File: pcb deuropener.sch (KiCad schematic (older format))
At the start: 30 parts, among them J1 Conn_01x02, J10 Conn_01x03, J11 Barrel_Jack_Switch, J12 Conn_01x08, J13 Conn_01x02, J14 Conn_01x02, J2 Conn_01x02, J3 Conn_01x02, J4 Conn_01x02, J8 Conn_01x02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

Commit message: A lot of changes to rev 0.02
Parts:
- removed J8: Conn_01x02, Connector_PinHeader_2.54mm:PinHeader_1x02_P2.54mm_Vertical, symbol Connector_Generic:Conn_01x02
- removed R11: R, Resistor_THT:R_Axial_DIN0207_L6.3mm_D2.5mm_P10.16mm_Horizontal, symbol Device:R
- added D3: LED, LED_THT:LED_D5.0mm, symbol Device:LED
- added D4: 1N4007, Diode_THT:D_DO-41_SOD81_P10.16mm_Horizontal, symbol Diode:1N4007
- added J5: Conn_01x02, Connector_PinHeader_2.54mm:PinHeader_1x02_P2.54mm_Vertical, symbol Connector_Generic:Conn_01x02
- added Q2: STU60N3LH5, Package_TO_SOT_THT:SIPAK_Vertical, symbol Device:Q_NMOS_GDS
- added R7, R8: R, Resistor_THT:R_Axial_DIN0207_L6.3mm_D2.5mm_P10.16mm_Horizontal, symbol Device:R
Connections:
- net +12V: now also D4.1 (K), J5.1 (Pin_1)
- net Earth: now also D3.1 (K), Q2.3 (S)
- net IO-P9_12-Solenoid: now reaches P9.12 (Pin_12)
- net IO-P9_12-Solenoid: now also R16.1, R17.1
- net IO-P9_16-UILED2: now reaches P9.16 (Pin_16)
- net IO-P9_16-UILED2: now also R4.1
- net IO-P8_13-UI_TriLED1r: now reaches P8.13 (Pin_13)
- net IO-P8_13-UI_TriLED1r: now also R14.2
- net IO-P8_17-Button1: now reaches P8.17 (Pin_17)
- net IO-P8_17-Button1: now also C2.2, R5.2, R6.1
- net IO-P8_18-Button2: now reaches P8.18 (Pin_18)
- net IO-P8_18-Button2: now also C1.2, R2.2, R3.1
- net IO-P8_19-UI_TriLED1g: now reaches P8.19 (Pin_19)
- net IO-P8_19-UI_TriLED1g: now also R15.2
- net IO-P8_09-Buzzer: now reaches P8.9 (Pin_9)
- net IO-P8_09-Buzzer: now also R7.1, R8.1
- removed net IO-P8_21-Button2: C1.2, P8.21 (Pin_21), R2.2, R3.1
- removed net IO-P8_23-Button1: C2.2, P8.23 (Pin_23), R5.2, R6.1
- net IO-P8_34-UILED1: no longer names the net of P8.34 (Pin_34)
- net IO-P8_34-UILED1: no longer R1.1
- net IO-P8_36-UILED2: no longer names the net of P8.36 (Pin_36)
- net IO-P8_36-UILED2: no longer R4.1
- net IO-P8_45-UI_BiLED1g: no longer names the net of P8.45 (Pin_45)
- net IO-P8_46-UI_BiLED1r: no longer names the net of P8.46 (Pin_46)
- removed net IO-P9_14-Solenoid: P9.14 (Pin_14), R16.1, R17.1
- net IO-P9_28-UI_TriLED1r: no longer names the net of P9.28 (Pin_28)
- net IO-P9_28-UI_TriLED1r: no longer R14.2
- net IO-P9_42-UI_TriLED1g: no longer names the net of P9.42 (Pin_42)
- net IO-P9_42-UI_TriLED1g: no longer R15.2
- new net: D3.2 (A), R7.2
- new net: Q2.1 (G), R8.2
- new net: D4.2 (A), J5.2 (Pin_2), Q2.2 (D)
- new net IO-P9_14-UILED1: P9.14 (Pin_14), R1.1
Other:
- note added: "Buzzer 12V"
- note added: "Doorbell (button2)"
- note added: "intercom door open switch \n(Button1)"
- note removed: "Button 1"
- note removed: "Button 2"
- note removed: "UI bicolor LED"
- moved on the sheet: C3, D1, D2, J10, J13, Q1, R14, R15, R16, R17

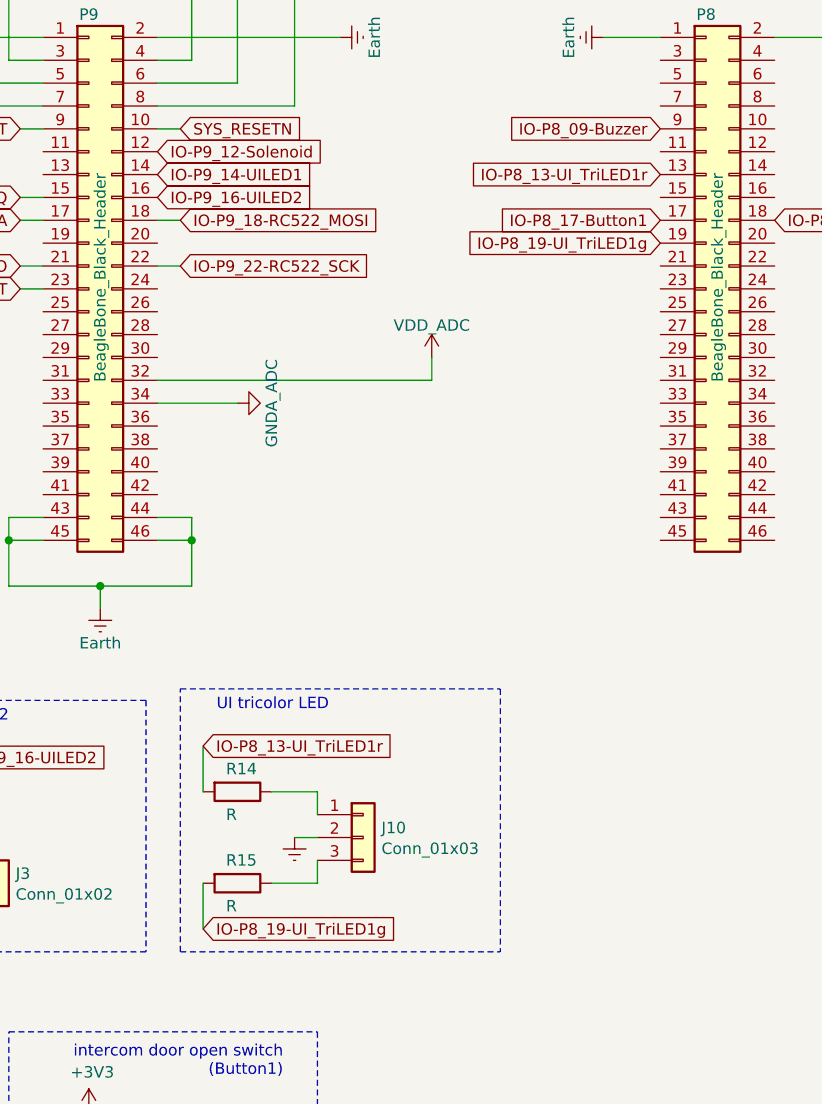
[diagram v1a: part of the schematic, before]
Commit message: A lot of changes for rev0.02 and fix for issue #2
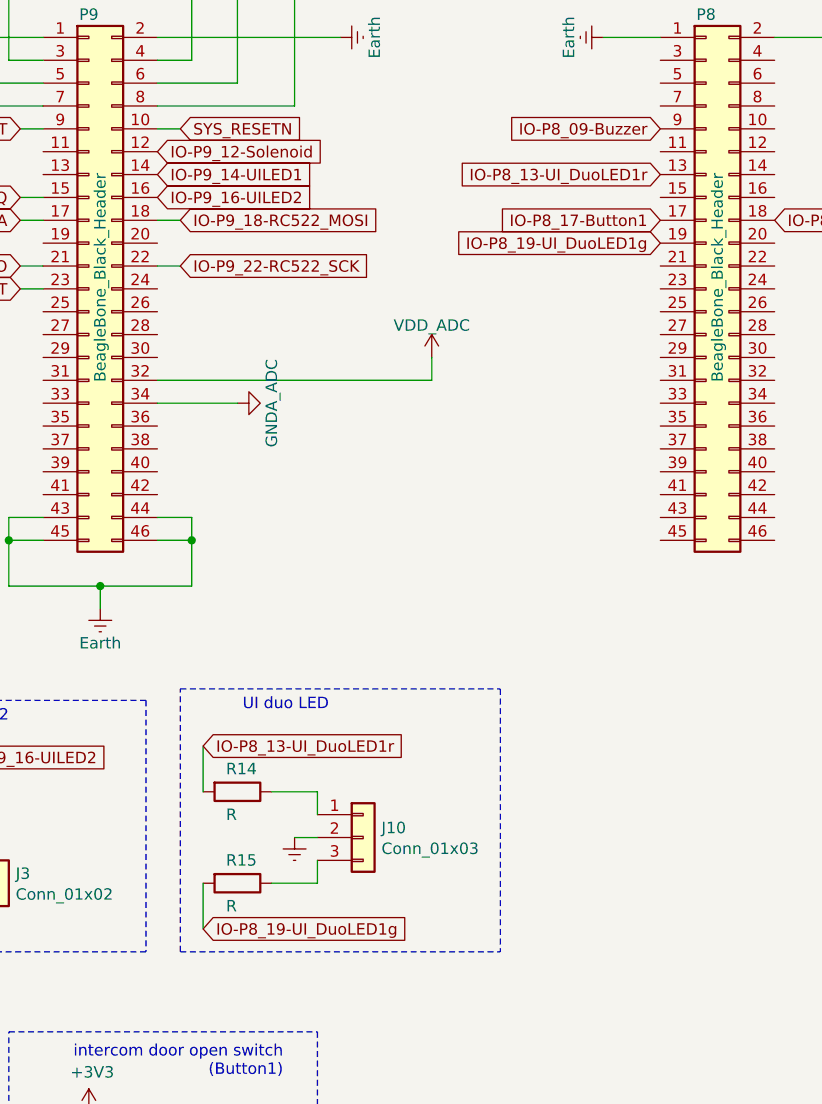
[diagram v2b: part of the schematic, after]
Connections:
- net IO-P8_13-UI_TriLED1r renamed IO-P8_13-UI_DuoLED1r
- net IO-P8_19-UI_TriLED1g renamed IO-P8_19-UI_DuoLED1g
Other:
- note added: "UI duo LED"
- note removed: "UI tricolor LED"
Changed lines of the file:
@@
 $EndComp
 Text GLabel 2900 4250 2    50   Input ~ 0
-IO-P8_13-UI_TriLED1r
+IO-P8_13-UI_DuoLED1r
 Text Notes 3450 4100 2    50   ~ 0
-UI tricolor LED
+UI duo LED
 Text GLabel 2900 5050 2    50   Input ~ 0
-IO-P8_19-UI_TriLED1g
+IO-P8_19-UI_DuoLED1g
 Wire Notes Line
 	2800 5150 2800 4000
@@
 IO-P9_16-UILED2
 Text GLabel 4900 1750 0    50   Input ~ 0
-IO-P8_13-UI_TriLED1r
+IO-P8_13-UI_DuoLED1r
 Text GLabel 4900 2050 0    50   Input ~ 0
-IO-P8_19-UI_TriLED1g
+IO-P8_19-UI_DuoLED1g
 Text GLabel 5400 1950 2    50   Input ~ 0
 IO-P8_18-Button2

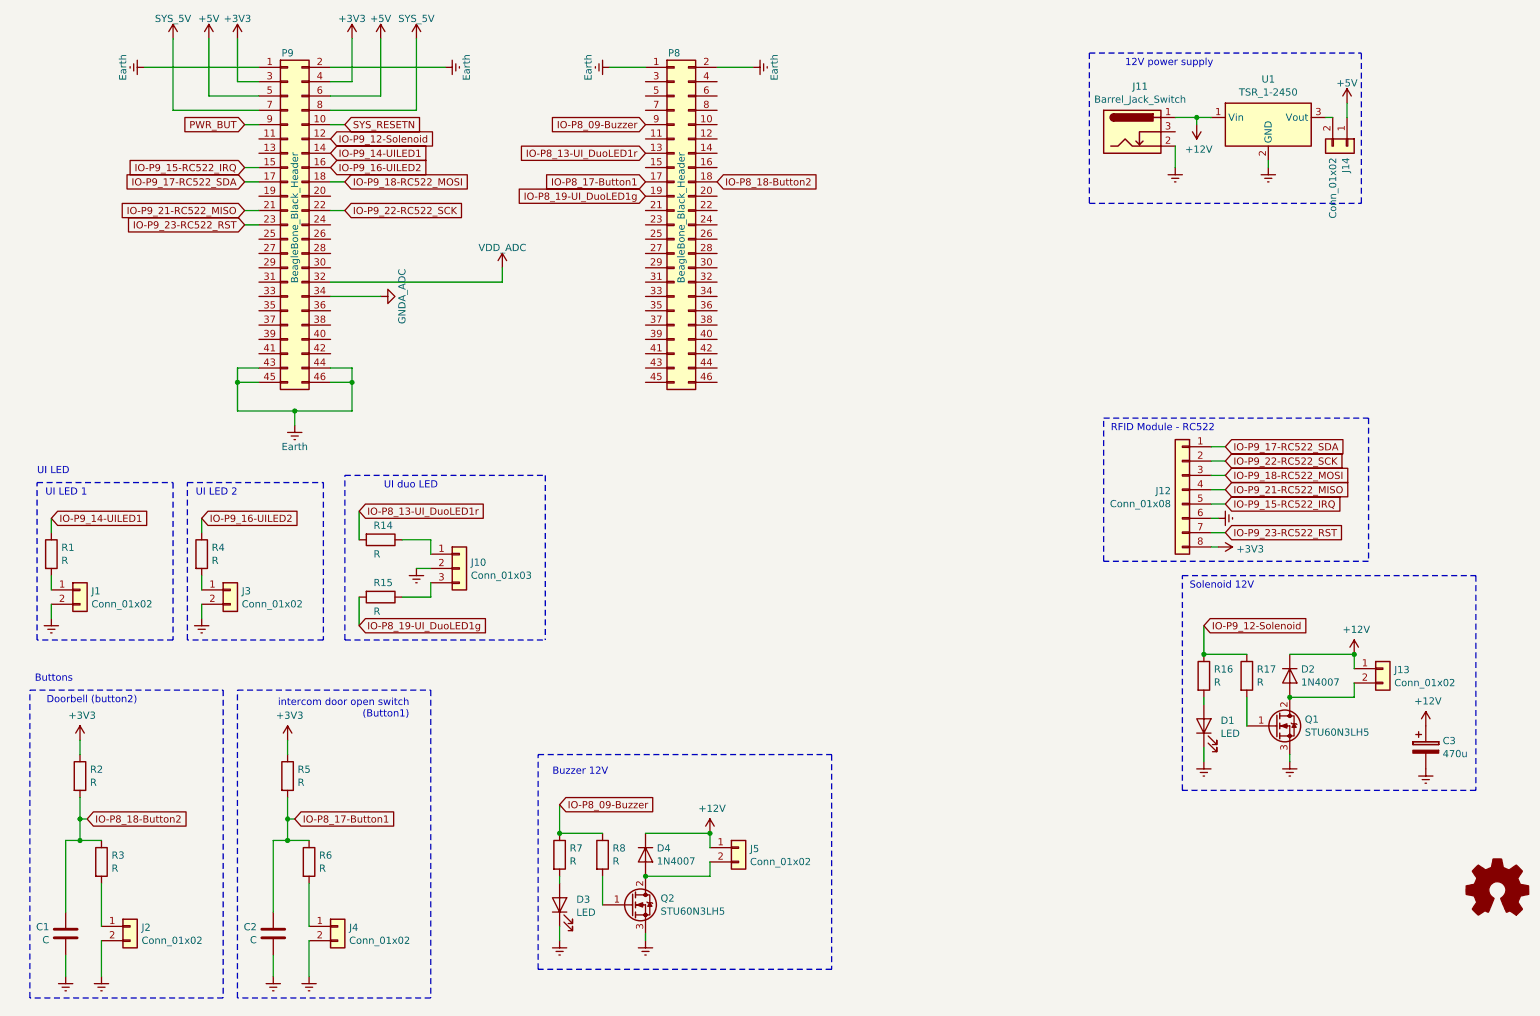
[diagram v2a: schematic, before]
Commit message: Documentation file added with GPIO port information and component list with values. in info_rev0.01.txt
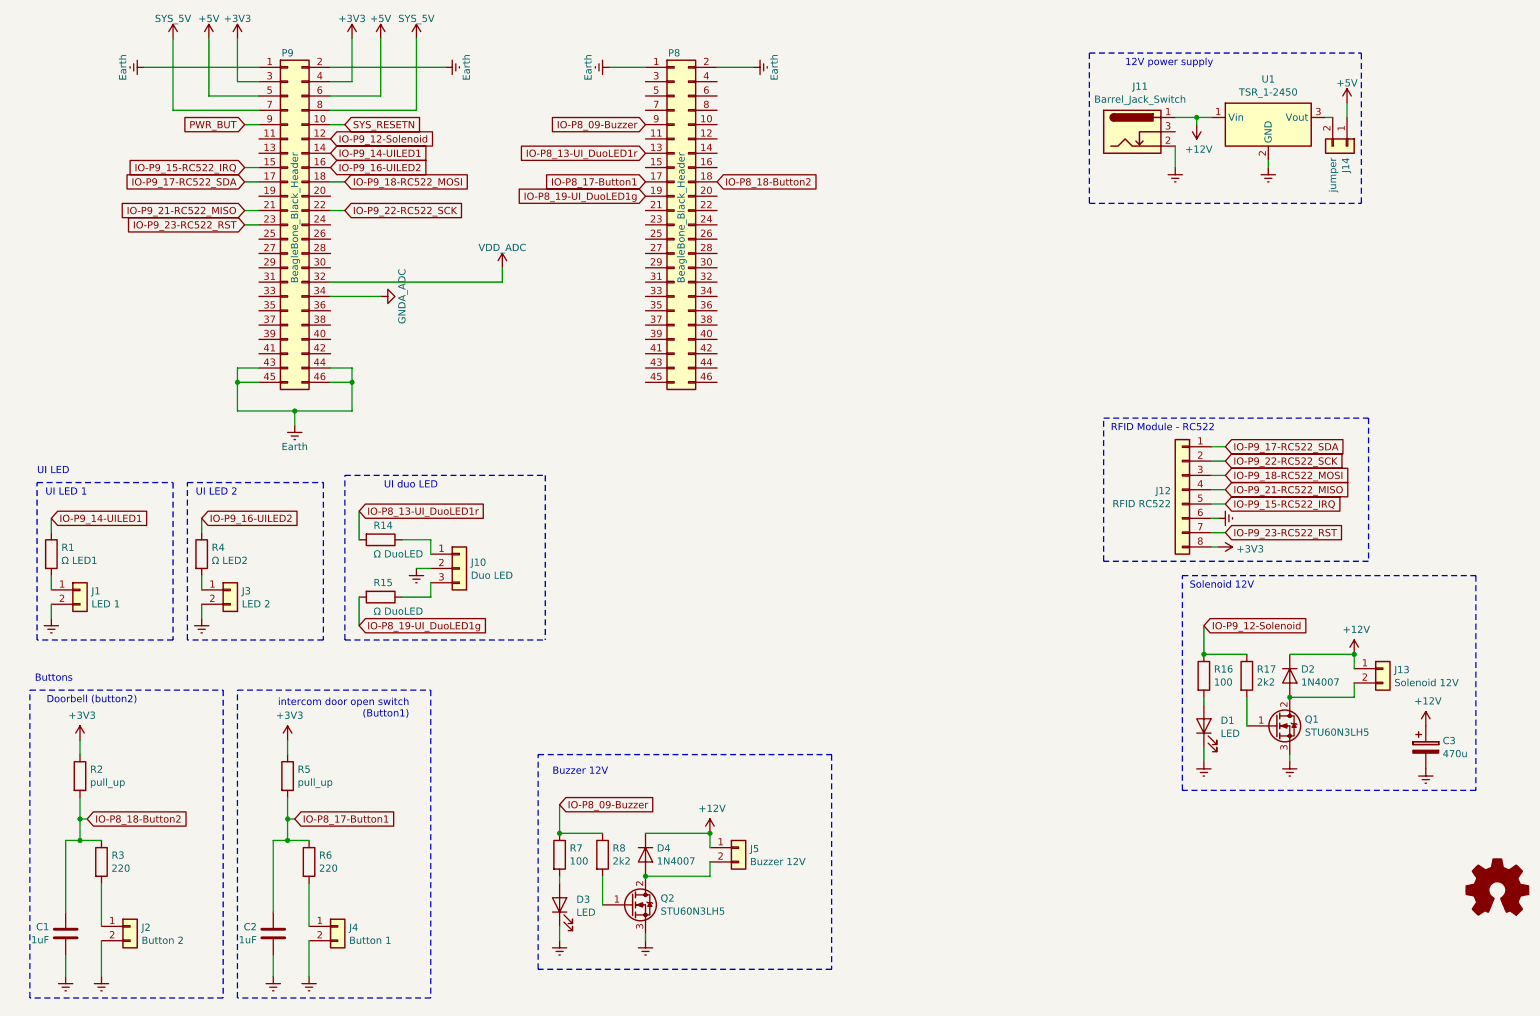
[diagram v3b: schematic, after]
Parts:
- C1, C2: value C -> 1uF
- J1: value Conn_01x02 -> LED 1
- J10: value Conn_01x03 -> Duo LED
- J12: value Conn_01x08 -> RFID RC522
- J13: value Conn_01x02 -> Solenoid 12V
- J14: value Conn_01x02 -> jumper
- J2: value Conn_01x02 -> Button 2
- J3: value Conn_01x02 -> LED 2
- J4: value Conn_01x02 -> Button 1
- J5: value Conn_01x02 -> Buzzer 12V
- R1: value R -> Ω LED1
- R14, R15: value R -> Ω DuoLED
- R16, R7: value R -> 100
- R17, R8: value R -> 2k2
- R2, R5: value R -> pull_up
- R3, R6: value R -> 220
- R4: value R -> Ω LED2
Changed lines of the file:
@@
 P 8800 5400
 F 0 "R16" H 8870 5446 50  0000 L CNN
-F 1 "R" H 8870 5355 50  0000 L CNN
+F 1 "100" H 8870 5355 50  0000 L CNN
 F 2 "Resistor_THT:R_Axial_DIN0207_L6.3mm_D2.5mm_P10.16mm_Horizontal" V 8730 5400 50  0001 C CNN
 F 3 "~" H 8800 5400 50  0001 C CNN
@@
 P 9100 5400
 F 0 "R17" H 9170 5446 50  0000 L CNN
-F 1 "R" H 9170 5355 50  0000 L CNN
+F 1 "2k2" H 9170 5355 50  0000 L CNN
 F 2 "Resistor_THT:R_Axial_DIN0207_L6.3mm_D2.5mm_P10.16mm_Horizontal" V 9030 5400 50  0001 C CNN
 F 3 "~" H 9100 5400 50  0001 C CNN
@@
 P 10050 5350
 F 0 "J13" H 10130 5342 50  0000 L CNN
-F 1 "Conn_01x02" H 10130 5251 50  0000 L CNN
+F 1 "Solenoid 12V" H 10130 5251 50  0000 L CNN
 F 2 "Connector_PinHeader_2.54mm:PinHeader_1x02_P2.54mm_Vertical" H 10050 5350 50  0001 C CNN
 F 3 "~" H 10050 5350 50  0001 C CNN
@@
 P 750 4550
 F 0 "R1" H 820 4596 50  0000 L CNN
-F 1 "R" H 820 4505 50  0000 L CNN
+F 1 "Ω LED1 " H 820 4505 50  0000 L CNN
 F 2 "Resistor_THT:R_Axial_DIN0207_L6.3mm_D2.5mm_P10.16mm_Horizontal" V 680 4550 50  0001 C CNN
 F 3 "~" H 750 4550 50  0001 C CNN
@@
 P 950 4800
 F 0 "J1" H 1030 4792 50  0000 L CNN
-F 1 "Conn_01x02" H 1030 4701 50  0000 L CNN
+F 1 "LED 1" H 1030 4701 50  0000 L CNN
 F 2 "Connector_PinHeader_2.54mm:PinHeader_1x02_P2.54mm_Vertical" H 950 4800 50  0001 C CNN
 F 3 "~" H 950 4800 50  0001 C CNN
@@
 P 950 6100
 F 0 "R2" H 1020 6146 50  0000 L CNN
-F 1 "R" H 1020 6055 50  0000 L CNN
+F 1 "pull_up" H 1020 6055 50  0000 L CNN
 F 2 "Resistor_THT:R_Axial_DIN0207_L6.3mm_D2.5mm_P10.16mm_Horizontal" V 880 6100 50  0001 C CNN
 F 3 "~" H 950 6100 50  0001 C CNN
@@
 P 1100 6700
 F 0 "R3" H 1170 6746 50  0000 L CNN
-F 1 "R" H 1170 6655 50  0000 L CNN
+F 1 "220" H 1170 6655 50  0000 L CNN
 F 2 "Resistor_THT:R_Axial_DIN0207_L6.3mm_D2.5mm_P10.16mm_Horizontal" V 1030 6700 50  0001 C CNN
 F 3 "~" H 1100 6700 50  0001 C CNN
@@
 P 850 7200
 F 0 "C1" H 735 7154 50  0000 R CNN
-F 1 "C" H 735 7245 50  0000 R CNN
+F 1 "1uF " H 735 7245 50  0000 R CNN
 F 2 "Capacitor_THT:C_Disc_D7.5mm_W4.4mm_P5.00mm" H 888 7050 50  0001 C CNN
 F 3 "~" H 850 7200 50  0001 C CNN
@@
 P 1300 7150
 F 0 "J2" H 1380 7142 50  0000 L CNN
-F 1 "Conn_01x02" H 1380 7051 50  0000 L CNN
+F 1 "Button 2" H 1380 7051 50  0000 L CNN
 F 2 "Connector_PinHeader_2.54mm:PinHeader_1x02_P2.54mm_Vertical" H 1300 7150 50  0001 C CNN
 F 3 "~" H 1300 7150 50  0001 C CNN
@@
 P 8650 4100
 F 0 "J12" H 8730 4092 50  0000 L CNN
-F 1 "Conn_01x08" H 8730 4001 50  0000 L CNN
+F 1 "RFID RC522" H 8730 4001 50  0000 L CNN
 F 2 "Connector_PinHeader_2.54mm:PinHeader_1x08_P2.54mm_Vertical" H 8650 4100 50  0001 C CNN
 F 3 "~" H 8650 4100 50  0001 C CNN
@@
 P 3050 4450
 F 0 "R14" V 2950 4400 50  0000 L CNN
-F 1 "R" V 3150 4400 50  0000 L CNN
+F 1 "Ω DuoLED" V 3150 4400 50  0000 L CNN
 F 2 "Resistor_THT:R_Axial_DIN0207_L6.3mm_D2.5mm_P10.16mm_Horizontal" V 2980 4450 50  0001 C CNN
 F 3 "~" H 3050 4450 50  0001 C CNN
@@
 P 3050 4850
 F 0 "R15" V 2950 4800 50  0000 L CNN
-F 1 "R" V 3150 4800 50  0000 L CNN
+F 1 "Ω DuoLED" V 3150 4800 50  0000 L CNN
 F 2 "Resistor_THT:R_Axial_DIN0207_L6.3mm_D2.5mm_P10.16mm_Horizontal" V 2980 4850 50  0001 C CNN
 F 3 "~" H 3050 4850 50  0001 C CNN
@@
 P 3600 4650
 F 0 "J10" H 3680 4692 50  0000 L CNN
-F 1 "Conn_01x03" H 3680 4601 50  0000 L CNN
+F 1 "Duo LED" H 3680 4601 50  0000 L CNN
 F 2 "Connector_PinHeader_2.54mm:PinHeader_1x03_P2.54mm_Vertical" H 3600 4650 50  0001 C CNN
 F 3 "~" H 3600 4650 50  0001 C CNN
@@
 P 1800 4550
 F 0 "R4" H 1870 4596 50  0000 L CNN
-F 1 "R" H 1870 4505 50  0000 L CNN
+F 1 "Ω LED2" H 1870 4505 50  0000 L CNN
 F 2 "Resistor_THT:R_Axial_DIN0207_L6.3mm_D2.5mm_P10.16mm_Horizontal" V 1730 4550 50  0001 C CNN
 F 3 "~" H 1800 4550 50  0001 C CNN
@@
 P 2000 4800
 F 0 "J3" H 2080 4792 50  0000 L CNN
-F 1 "Conn_01x02" H 2080 4701 50  0000 L CNN
+F 1 "LED 2" H 2080 4701 50  0000 L CNN
 F 2 "Connector_PinHeader_2.54mm:PinHeader_1x02_P2.54mm_Vertical" H 2000 4800 50  0001 C CNN
 F 3 "~" H 2000 4800 50  0001 C CNN
@@
 P 9800 1700
 F 0 "J14" H 9880 1692 50  0000 L CNN
-F 1 "Conn_01x02" H 9880 1601 50  0000 L CNN
+F 1 "jumper" H 9880 1601 50  0000 L CNN
 F 2 "Connector_PinHeader_2.54mm:PinHeader_1x02_P2.54mm_Vertical" H 9800 1700 50  0001 C CNN
 F 3 "~" H 9800 1700 50  0001 C CNN
@@
 P 2400 6100
 F 0 "R5" H 2470 6146 50  0000 L CNN
-F 1 "R" H 2470 6055 50  0000 L CNN
+F 1 "pull_up" H 2470 6055 50  0000 L CNN
 F 2 "Resistor_THT:R_Axial_DIN0207_L6.3mm_D2.5mm_P10.16mm_Horizontal" V 2330 6100 50  0001 C CNN
 F 3 "~" H 2400 6100 50  0001 C CNN
@@
 P 2550 6700
 F 0 "R6" H 2620 6746 50  0000 L CNN
-F 1 "R" H 2620 6655 50  0000 L CNN
+F 1 "220" H 2620 6655 50  0000 L CNN
 F 2 "Resistor_THT:R_Axial_DIN0207_L6.3mm_D2.5mm_P10.16mm_Horizontal" V 2480 6700 50  0001 C CNN
 F 3 "~" H 2550 6700 50  0001 C CNN
@@
 P 2300 7200
 F 0 "C2" H 2185 7154 50  0000 R CNN
-F 1 "C" H 2185 7245 50  0000 R CNN
+F 1 "1uF" H 2185 7245 50  0000 R CNN
 F 2 "Capacitor_THT:C_Disc_D7.5mm_W4.4mm_P5.00mm" H 2338 7050 50  0001 C CNN
 F 3 "~" H 2300 7200 50  0001 C CNN
@@
 P 2750 7150
 F 0 "J4" H 2830 7142 50  0000 L CNN
-F 1 "Conn_01x02" H 2830 7051 50  0000 L CNN
+F 1 "Button 1" H 2830 7051 50  0000 L CNN
 F 2 "Connector_PinHeader_2.54mm:PinHeader_1x02_P2.54mm_Vertical" H 2750 7150 50  0001 C CNN
 F 3 "~" H 2750 7150 50  0001 C CNN
@@
 P 4300 6650
 F 0 "R7" H 4370 6696 50  0000 L CNN
-F 1 "R" H 4370 6605 50  0000 L CNN
+F 1 "100" H 4370 6605 50  0000 L CNN
 F 2 "Resistor_THT:R_Axial_DIN0207_L6.3mm_D2.5mm_P10.16mm_Horizontal" V 4230 6650 50  0001 C CNN
 F 3 "~" H 4300 6650 50  0001 C CNN
@@
 P 4600 6650
 F 0 "R8" H 4670 6696 50  0000 L CNN
-F 1 "R" H 4670 6605 50  0000 L CNN
+F 1 "2k2" H 4670 6605 50  0000 L CNN
 F 2 "Resistor_THT:R_Axial_DIN0207_L6.3mm_D2.5mm_P10.16mm_Horizontal" V 4530 6650 50  0001 C CNN
 F 3 "~" H 4600 6650 50  0001 C CNN
@@
 P 5550 6600
 F 0 "J5" H 5630 6592 50  0000 L CNN
-F 1 "Conn_01x02" H 5630 6501 50  0000 L CNN
+F 1 "Buzzer 12V" H 5630 6501 50  0000 L CNN
 F 2 "Connector_PinHeader_2.54mm:PinHeader_1x02_P2.54mm_Vertical" H 5550 6600 50  0001 C CNN
 F 3 "~" H 5550 6600 50  0001 C CNN
